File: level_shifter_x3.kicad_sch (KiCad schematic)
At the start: 0 parts

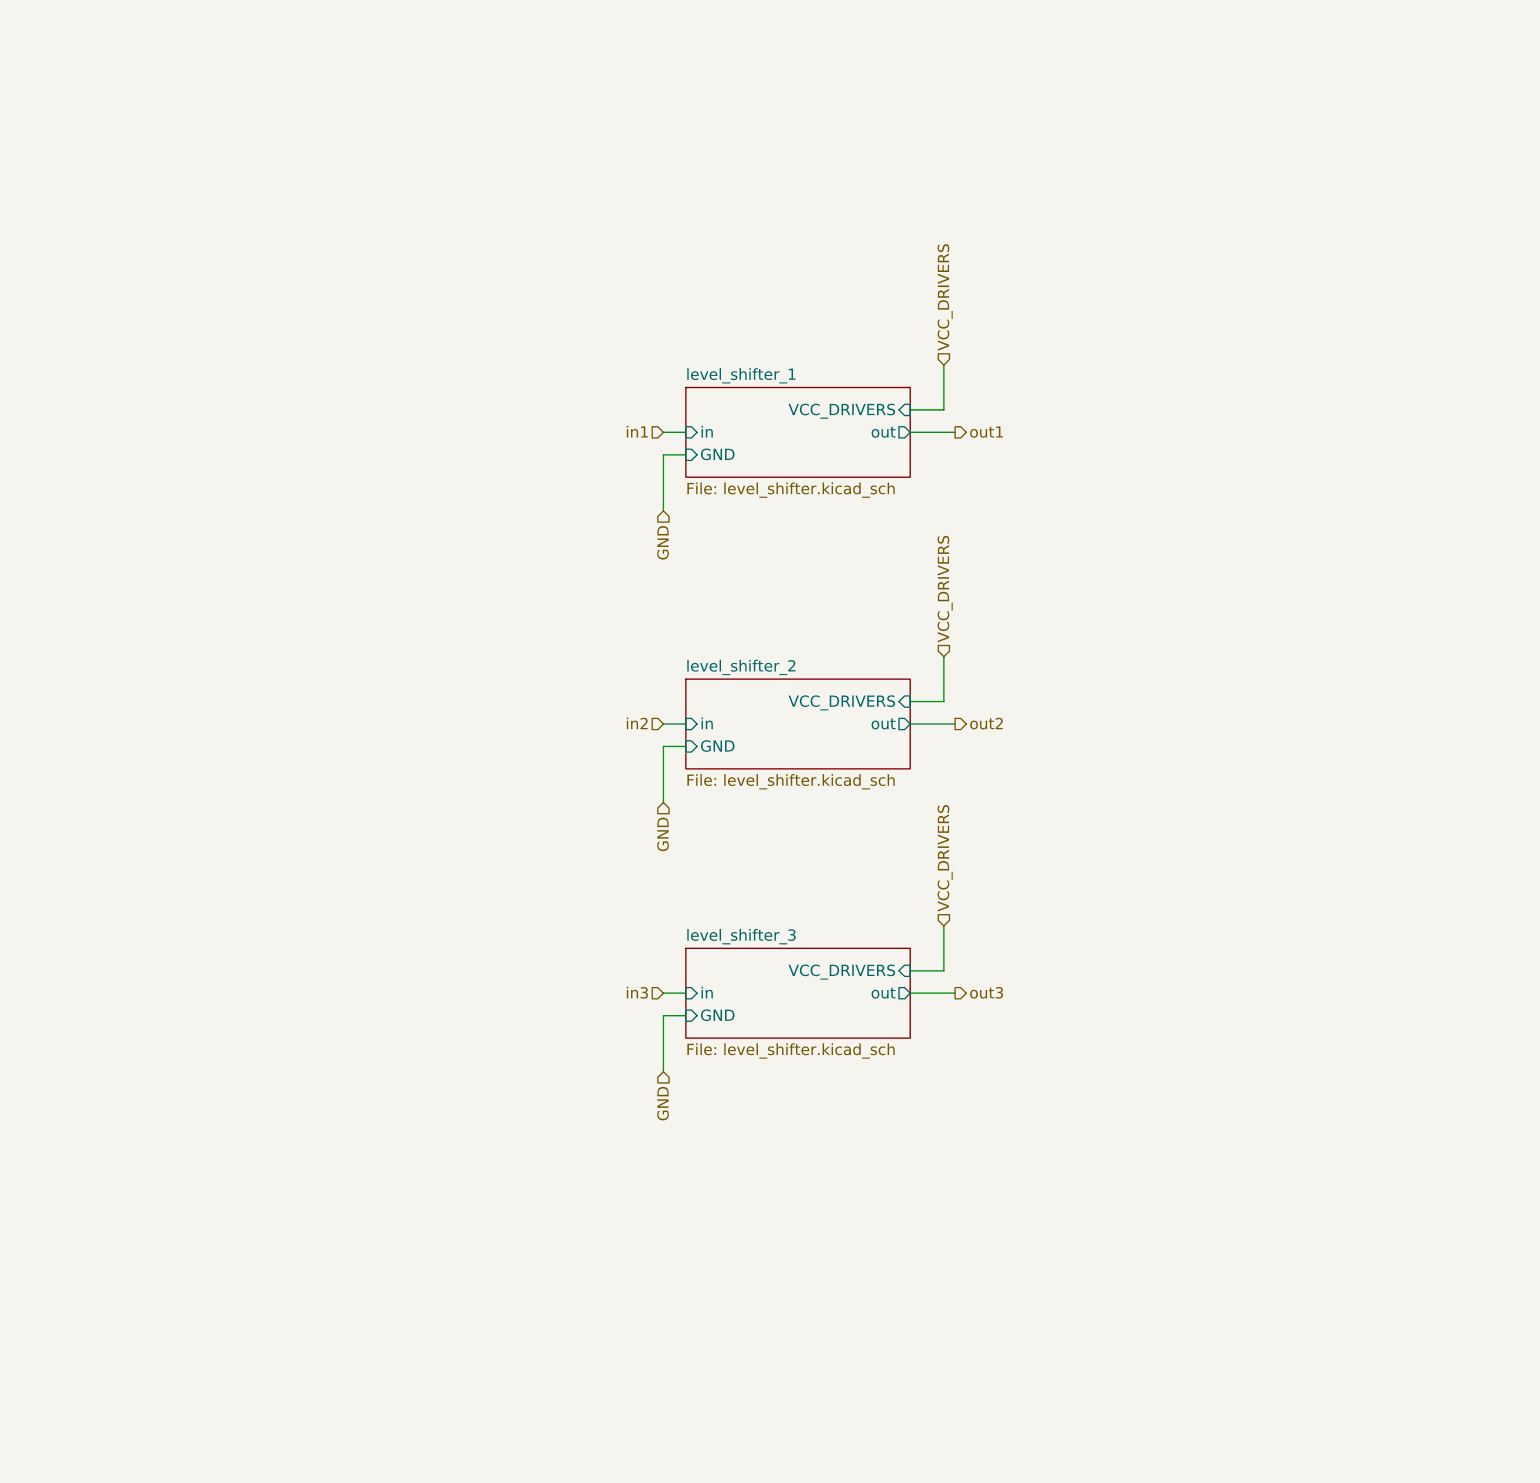
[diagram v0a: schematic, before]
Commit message: Refactored top sheet
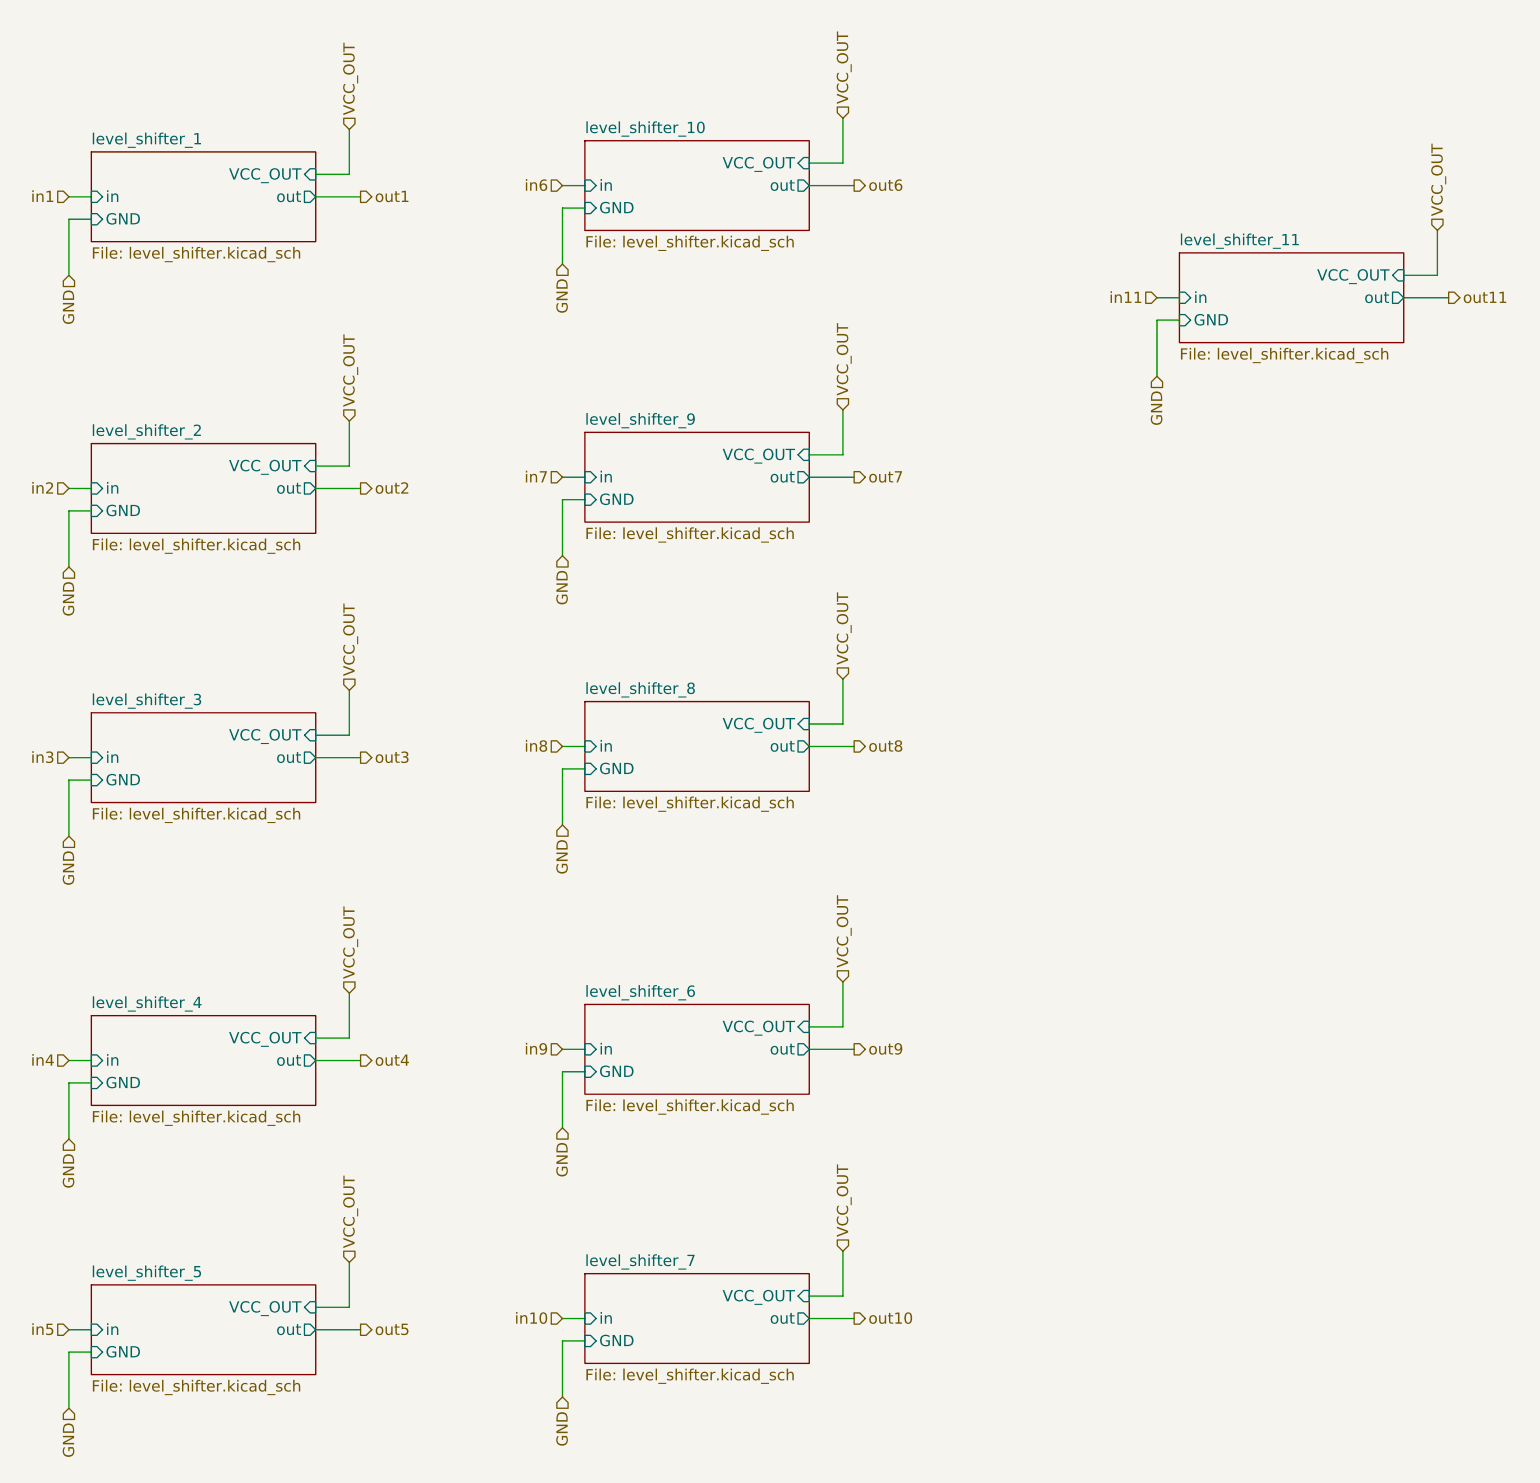
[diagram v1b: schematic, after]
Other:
- added sheet level_shifter_10 (level_shifter.kicad_sch)
- added sheet level_shifter_11 (level_shifter.kicad_sch)
- added sheet level_shifter_4 (level_shifter.kicad_sch)
- added sheet level_shifter_5 (level_shifter.kicad_sch)
- added sheet level_shifter_6 (level_shifter.kicad_sch)
- added sheet level_shifter_7 (level_shifter.kicad_sch)
- added sheet level_shifter_8 (level_shifter.kicad_sch)
- added sheet level_shifter_9 (level_shifter.kicad_sch)
- sheet level_shifter_1 ports: added VCC_OUT; removed VCC_DRIVERS
- sheet level_shifter_2 ports: added VCC_OUT; removed VCC_DRIVERS
- sheet level_shifter_3 ports: added VCC_OUT; removed VCC_DRIVERS
